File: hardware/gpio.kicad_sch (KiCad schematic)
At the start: 14 parts, among them U4 CCGM1A1

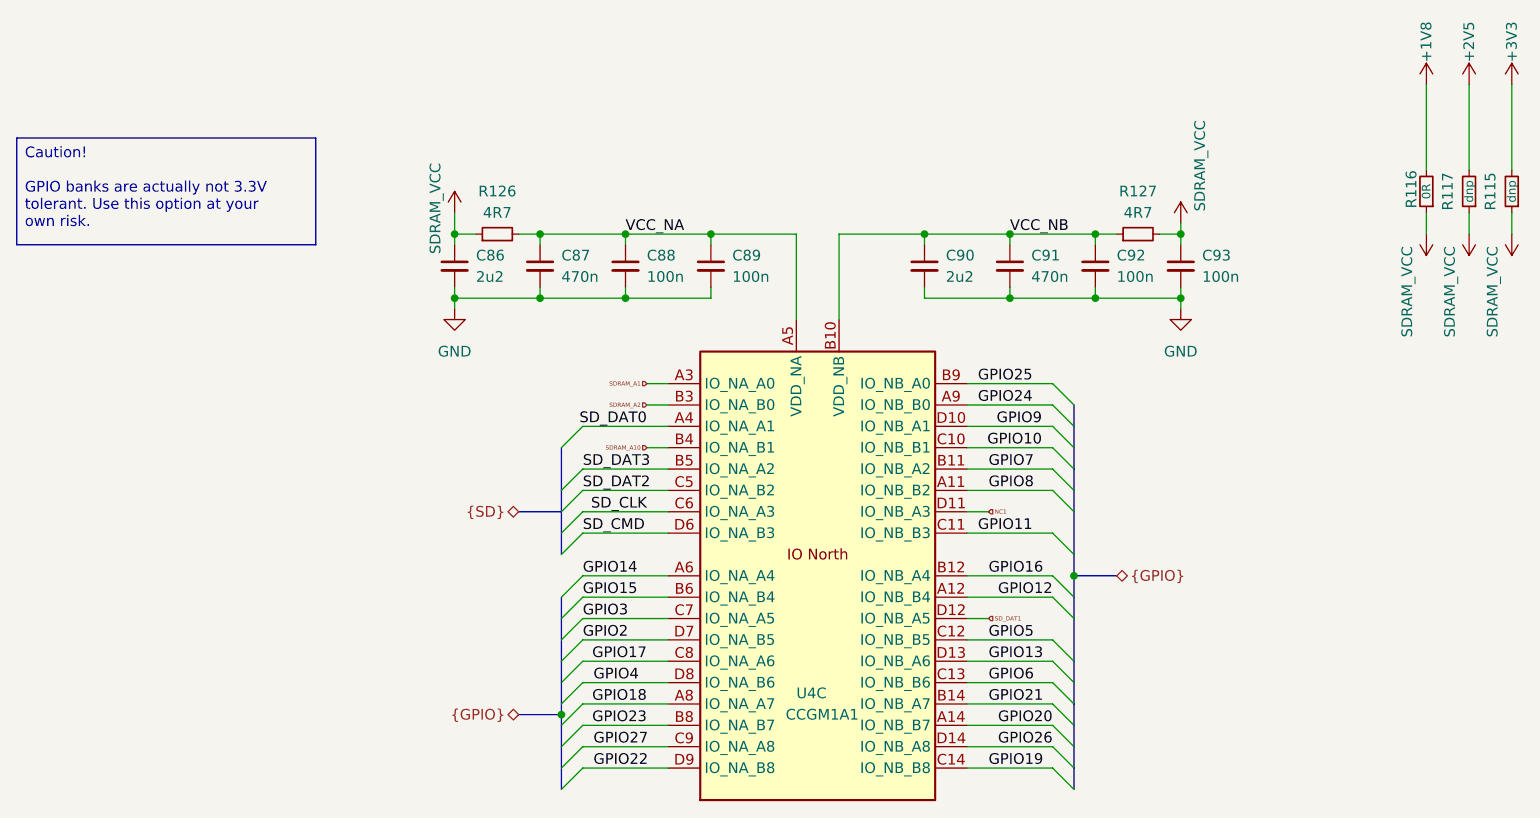
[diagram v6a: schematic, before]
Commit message: Clearing ERC errors/warnings
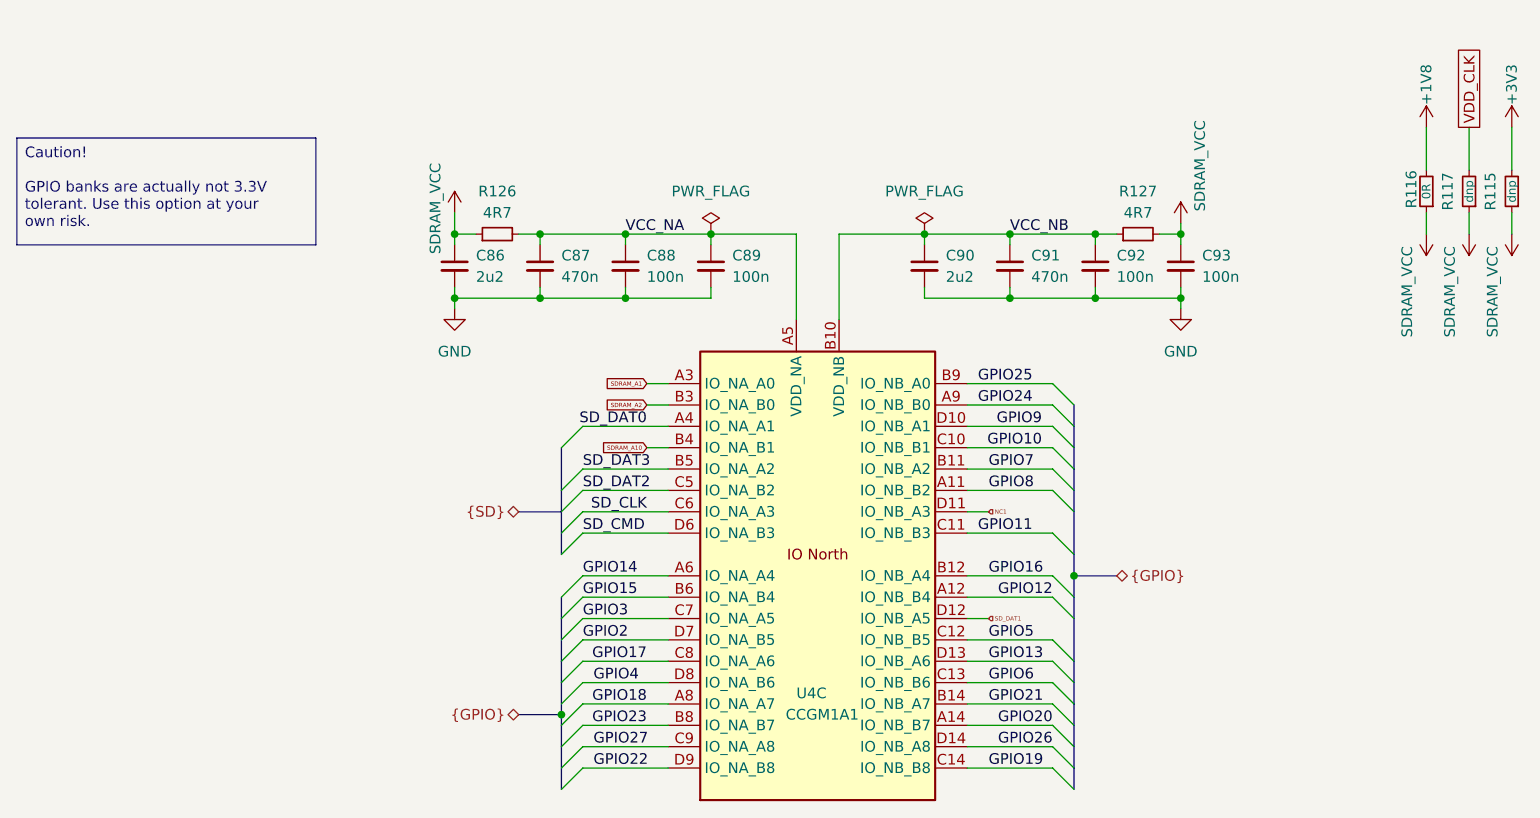
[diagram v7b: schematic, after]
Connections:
- net +2V5 renamed VDD_CLK
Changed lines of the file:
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@@
 	(wire
 		(pts
-			(xy 234.95 20.32) (xy 234.95 30.48)
+			(xy 234.95 25.4) (xy 234.95 30.48)
 		)
 		(stroke
@@
 	(wire
 		(pts
-			(xy 224.79 30.48) (xy 224.79 20.32)
+			(xy 224.79 30.48) (xy 224.79 25.4)
 		)
 		(stroke
@@
 	(wire
 		(pts
-			(xy 229.87 20.32) (xy 229.87 30.48)
+			(xy 229.87 25.4) (xy 229.87 30.48)
 		)
 		(stroke
@@
 		)
 	)
-	(hierarchical_label "{SD}"
-		(shape bidirectional)
-		(at 116.84 71.12 180)
+	(global_label "SDRAM_A2"
+		(shape input)
+		(at 132.08 58.42 180)
+		(fields_autoplaced yes)
 		(effects
 			(font
-				(size 1.27 1.27)
+				(size 0.5 0.5)
 			)
 			(justify right)
 		)
+		(property "Intersheetrefs" "${INTERSHEET_REFS}"
+			(at 127.1427 58.42 0)
+			(effects
+				(font
+					(size 1.27 1.27)
+				)
+				(justify right)
+				(hide yes)
+			)
+		)
 	)
-	(hierarchical_label "SDRAM_A10"
+	(global_label "VDD_CLK"
+		(shape passive)
+		(at 229.87 25.4 90)
+		(fields_autoplaced yes)
+		(effects
+			(font
+				(size 1.27 1.27)
+			)
+			(justify left)
+		)
+		(property "Intersheetrefs" "${INTERSHEET_REFS}"
+			(at 229.87 15.3618 90)
+			(effects
+				(font
+					(size 1.27 1.27)
+				)
+				(justify left)
+				(hide yes)
+			)
+		)
+	)
+	(global_label "SDRAM_A10"
 		(shape input)
 		(at 132.08 63.5 180)
+		(fields_autoplaced yes)
 		(effects
 			(font
@@
 			(justify right)
 		)
+		(property "Intersheetrefs" "${INTERSHEET_REFS}"
+			(at 126.6665 63.5 0)
+			(effects
+				(font
+					(size 1.27 1.27)
+				)
+				(justify right)
+				(hide yes)
+			)
+		)
 	)
-	(hierarchical_label "SDRAM_A2"
+	(global_label "SDRAM_A1"
 		(shape input)
-		(at 132.08 58.42 180)
+		(at 132.08 55.88 180)
+		(fields_autoplaced yes)
 		(effects
 			(font
@@
 			(justify right)
 		)
+		(property "Intersheetrefs" "${INTERSHEET_REFS}"
+			(at 127.1427 55.88 0)
+			(effects
+				(font
+					(size 1.27 1.27)
+				)
+				(justify right)
+				(hide yes)
+			)
+		)
 	)
-	(hierarchical_label "SD_DAT1"
-		(shape input)
-		(at 172.72 83.82 0)
+	(hierarchical_label "{SD}"
+		(shape bidirectional)
+		(at 116.84 71.12 180)
 		(effects
 			(font
-				(size 0.5 0.5)
+				(size 1.27 1.27)
 			)
-			(justify left)
+			(justify right)
 		)
 	)
-	(hierarchical_label "SDRAM_A1"
+	(hierarchical_label "SD_DAT1"
 		(shape input)
-		(at 132.08 55.88 180)
+		(at 172.72 83.82 0)
 		(effects
 			(font
 				(size 0.5 0.5)
 			)
-			(justify right)
+			(justify left)
 		)
 	)
@@
 			)
 		)
-		(property "Description" ""
+		(property "Description" "Resistor, small symbol"
 			(at 190.5 38.1 0)
 			(effects
@@
 					(size 1.27 1.27)
 				)
+				(hide yes)
 			)
 		)
@@
 	)
 	(symbol
-		(lib_id "power:+3V3")
-		(at 229.87 20.32 0)
+		(lib_id "power:PWR_FLAG")
+		(at 139.7 38.1 0)
 		(unit 1)
 		(exclude_from_sim no)
@@
 		(on_board yes)
 		(dnp no)
-		(property "Reference" "#PWR0136"
-			(at 229.87 24.13 0)
+		(fields_autoplaced yes)
+		(property "Reference" "#FLG017"
+			(at 139.7 36.195 0)
 			(effects
 				(font
@@
 			)
 		)
-		(property "Value" "+2V5"
-			(at 229.87 15.24 90)
+		(property "Value" "PWR_FLAG"
+			(at 139.7 33.02 0)
 			(effects
 				(font
@@
 		)
 		(property "Footprint" ""
-			(at 229.87 20.32 0)
+			(at 139.7 38.1 0)
 			(effects
 				(font
@@
 			)
 		)
-		(property "Datasheet" ""
-			(at 229.87 20.32 0)
+		(property "Datasheet" "~"
+			(at 139.7 38.1 0)
 			(effects
 				(font
@@
 			)
 		)
-		(property "Description" ""
-			(at 229.87 20.32 0)
+		(property "Description" "Special symbol for telling ERC where power comes from"
+			(at 139.7 38.1 0)
 			(effects
 				(font
 					(size 1.27 1.27)
 				)
+				(hide yes)
 			)
 		)
@@
 			(project "ulx5m-gs"
 				(path "/9e5cbfd6-8186-4817-919e-acd256336bc8/a29a432d-2cca-4e45-9947-735d9a1918bd"
-					(reference "#PWR0136")
+					(reference "#FLG017")
 					(unit 1)
 				)
@@
 	)
 	(symbol
-		(lib_name "R_Small_1")
 		(lib_id "Device:R_Small")
 		(at 229.87 33.02 180)
@@
 			)
 		)
-		(property "Description" ""
+		(property "Description" "Resistor, small symbol"
 			(at 229.87 33.02 0)
 			(effects
@@
 					(size 1.27 1.27)
 				)
+				(hide yes)
 			)
 		)
@@
 	)
 	(symbol
+		(lib_name "+3V3_1")
 		(lib_id "power:+3V3")
-		(at 234.95 20.32 0)
+		(at 234.95 25.4 0)
 		(unit 1)
 		(exclude_from_sim no)
@@
 		(dnp no)
 		(property "Reference" "#PWR0135"
-			(at 234.95 24.13 0)
+			(at 234.95 29.21 0)
 			(effects
 				(font
@@
 		)
 		(property "Value" "+3V3"
-			(at 234.95 15.24 90)
+			(at 234.95 20.32 90)
 			(effects
 				(font
@@
 		)
 		(property "Footprint" ""
-			(at 234.95 20.32 0)
+			(at 234.95 25.4 0)
 			(effects
 				(font
@@
 		)
 		(property "Datasheet" ""
-			(at 234.95 20.32 0)
+			(at 234.95 25.4 0)
 			(effects
 				(font
@@
 			)
 		)
-		(property "Description" ""
-			(at 234.95 20.32 0)
+		(property "Description" "Power symbol creates a global label with name \"+3V3\""
+			(at 234.95 25.4 0)
 			(effects
 				(font
 					(size 1.27 1.27)
 				)
+				(hide yes)
 			)
 		)
@@
 	)
 	(symbol
+		(lib_id "power:PWR_FLAG")
+		(at 165.1 38.1 0)
+		(unit 1)
+		(exclude_from_sim no)
+		(in_bom yes)
+		(on_board yes)
+		(dnp no)
+		(fields_autoplaced yes)
+		(property "Reference" "#FLG016"
+			(at 165.1 36.195 0)
+			(effects
+				(font
+					(size 1.27 1.27)
+				)
+				(hide yes)
+			)
+		)
+		(property "Value" "PWR_FLAG"
+			(at 165.1 33.02 0)
+			(effects
+				(font
+					(size 1.27 1.27)
+				)
+			)
+		)
+		(property "Footprint" ""
+			(at 165.1 38.1 0)
+			(effects
+				(font
+					(size 1.27 1.27)
+				)
+				(hide yes)
+			)
+		)
+		(property "Datasheet" "~"
+			(at 165.1 38.1 0)
+			(effects
+				(font
+					(size 1.27 1.27)
+				)
+				(hide yes)
+			)
+		)
+		(property "Description" "Special symbol for telling ERC where power comes from"
+			(at 165.1 38.1 0)
+			(effects
+				(font
+					(size 1.27 1.27)
+				)
+				(hide yes)
+			)
+		)
+		(pin "1"
+		)
+		(instances
+			(project ""
+				(path "/9e5cbfd6-8186-4817-919e-acd256336bc8/a29a432d-2cca-4e45-9947-735d9a1918bd"
+					(reference "#FLG016")
+					(unit 1)
+				)
+			)
+		)
+	)
+	(symbol
 		(lib_id "Device:R_Small")
 		(at 114.3 38.1 90)
@@
 			)
 		)
-		(property "Description" ""
+		(property "Description" "Resistor, small symbol"
 			(at 114.3 38.1 0)
 			(effects
@@
 					(size 1.27 1.27)
 				)
+				(hide yes)
 			)
 		)
@@
 			)
 		)
-		(property "Description" ""
+		(property "Description" "Power symbol creates a global label with name \"GND\" , ground"
 			(at 195.58 46.99 0)
 			(effects
@@
 					(size 1.27 1.27)
 				)
+				(hide yes)
 			)
 		)
@@
 	)
 	(symbol
-		(lib_name "R_Small_1")
 		(lib_id "Device:R_Small")
 		(at 234.95 33.02 180)
@@
 			)
 		)
-		(property "Description" ""
+		(property "Description" "Resistor, small symbol"
 			(at 234.95 33.02 0)
 			(effects
@@
 					(size 1.27 1.27)
 				)
+				(hide yes)
 			)
 		)
@@
 	(symbol
 		(lib_id "power:+1V8")
-		(at 224.79 20.32 0)
+		(at 224.79 25.4 0)
 		(unit 1)
 		(exclude_from_sim no)
@@
 		(dnp no)
 		(property "Reference" "#PWR091"
-			(at 224.79 24.13 0)
+			(at 224.79 29.21 0)
 			(effects
 				(font
@@
 		)
 		(property "Value" "+1V8"
-			(at 224.79 15.24 90)
+			(at 224.79 20.32 90)
 			(effects
 				(font
@@
 		)
 		(property "Footprint" ""
-			(at 224.79 20.32 0)
+			(at 224.79 25.4 0)
 			(effects
 				(font
@@
 		)
 		(property "Datasheet" ""
-			(at 224.79 20.32 0)
+			(at 224.79 25.4 0)
 			(effects
 				(font
@@
 			)
 		)
-		(property "Description" ""
-			(at 224.79 20.32 0)
+		(property "Description" "Power symbol creates a global label with name \"+1V8\""
+			(at 224.79 25.4 0)
 			(effects
 				(font
 					(size 1.27 1.27)
 				)
+				(hide yes)
 			)
 		)
@@
 			)
 		)
-		(property "Description" ""
+		(property "Description" "Power symbol creates a global label with name \"GND\" , ground"
 			(at 109.22 46.99 0)
 			(effects
@@
 					(size 1.27 1.27)
 				)
+				(hide yes)
 			)
 		)
@@
 			)
 		)
-		(property "Description" ""
+		(property "Description" "Resistor, small symbol"
 			(at 224.79 33.02 0)
 			(effects
@@
 					(size 1.27 1.27)
 				)
+				(hide yes)
 			)
 		)

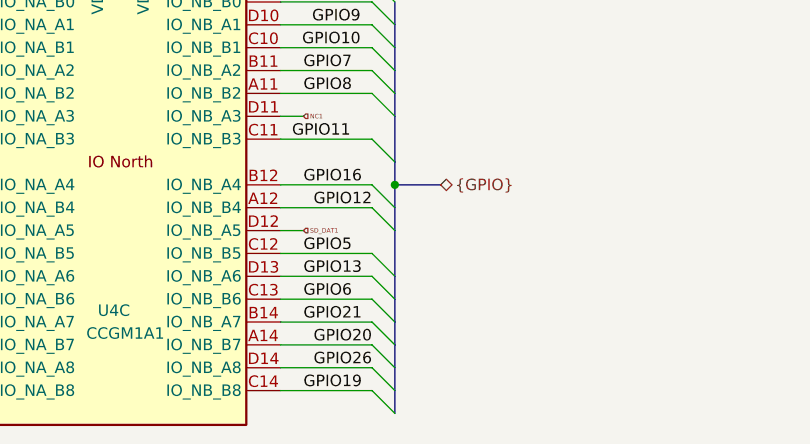
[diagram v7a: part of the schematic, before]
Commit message: Routing BTNs, LEDs, CLK
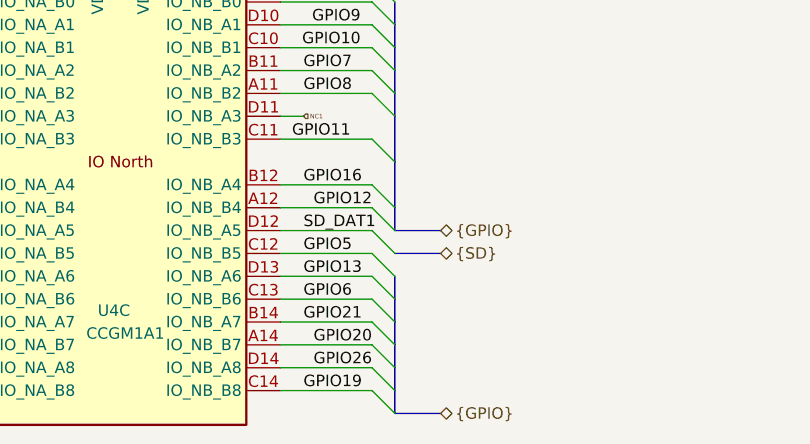
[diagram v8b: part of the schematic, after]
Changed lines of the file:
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@@
-	)
-	(junction
-		(at 182.88 78.74)
-		(diameter 0)
-		(color 0 0 0 0)
 	)
 	(junction
@@
 	)
 	(bus_entry
+		(at 180.34 83.82)
+		(size 2.54 2.54)
+		(stroke
+			(width 0)
+			(type default)
+		)
+	)
+	(bus_entry
 		(at 180.34 96.52)
 		(size 2.54 2.54)
@@
 	(wire
 		(pts
-			(xy 170.18 83.82) (xy 172.72 83.82)
+			(xy 170.18 83.82) (xy 180.34 83.82)
 		)
 		(stroke
@@
 	(bus
 		(pts
-			(xy 182.88 76.2) (xy 182.88 78.74)
+			(xy 182.88 76.2) (xy 182.88 81.28)
 		)
 		(stroke
@@
 		)
 	)
+	(bus
+		(pts
+			(xy 182.88 104.14) (xy 187.96 104.14)
+		)
+		(stroke
+			(width 0)
+			(type default)
+		)
+	)
 	(wire
 		(pts
@@
 	(bus
 		(pts
+			(xy 182.88 81.28) (xy 182.88 83.82)
+		)
+		(stroke
+			(width 0)
+			(type default)
+		)
+	)
+	(bus
+		(pts
 			(xy 182.88 88.9) (xy 182.88 91.44)
 		)
@@
 	(bus
 		(pts
+			(xy 182.88 86.36) (xy 187.96 86.36)
+		)
+		(stroke
+			(width 0)
+			(type default)
+		)
+	)
+	(bus
+		(pts
 			(xy 182.88 91.44) (xy 182.88 93.98)
 		)
@@
 		)
 	)
-	(bus
-		(pts
-			(xy 182.88 81.28) (xy 182.88 83.82)
-		)
-		(stroke
-			(width 0)
-			(type default)
-		)
-	)
 	(wire
 		(pts
@@
 	(bus
 		(pts
-			(xy 182.88 78.74) (xy 187.96 78.74)
+			(xy 182.88 83.82) (xy 187.96 83.82)
 		)
 		(stroke
@@
 		)
 	)
-	(bus
-		(pts
-			(xy 182.88 78.74) (xy 182.88 81.28)
-		)
-		(stroke
-			(width 0)
-			(type default)
-		)
-	)
 	(wire
 		(pts
@@
 		(pts
 			(xy 170.18 58.42) (xy 180.34 58.42)
-		)
-		(stroke
-			(width 0)
-			(type default)
-		)
-	)
-	(bus
-		(pts
-			(xy 182.88 83.82) (xy 182.88 88.9)
 		)
 		(stroke
@@
 	(label "GPIO5"
 		(at 172.72 86.36 0)
+		(effects
+			(font
+				(size 1.27 1.27)
+			)
+			(justify left bottom)
+		)
+	)
+	(label "SD_DAT1"
+		(at 172.72 83.82 0)
 		(effects
 			(font
@@
 		)
 	)
-	(hierarchical_label "SD_DAT1"
-		(shape input)
-		(at 172.72 83.82 0)
-		(effects
-			(font
-				(size 0.5 0.5)
+	(hierarchical_label "{SD}"
+		(shape bidirectional)
+		(at 187.96 86.36 0)
+		(effects
+			(font
+				(size 1.27 1.27)
+			)
+			(justify left)
+		)
+	)
+	(hierarchical_label "{GPIO}"
+		(shape bidirectional)
+		(at 187.96 104.14 0)
+		(effects
+			(font
+				(size 1.27 1.27)
 			)
 			(justify left)
@@
 	(hierarchical_label "{GPIO}"
 		(shape bidirectional)
-		(at 187.96 78.74 0)
-		(effects
-			(font
+		(at 187.96 83.82 0)
+		(effects
+			(font
